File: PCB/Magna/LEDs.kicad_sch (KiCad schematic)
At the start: 90 parts, among them U2001 74HC595, U2002 74HC595, U2003 74HC595, U2004 74HC595, U2005 74HC595

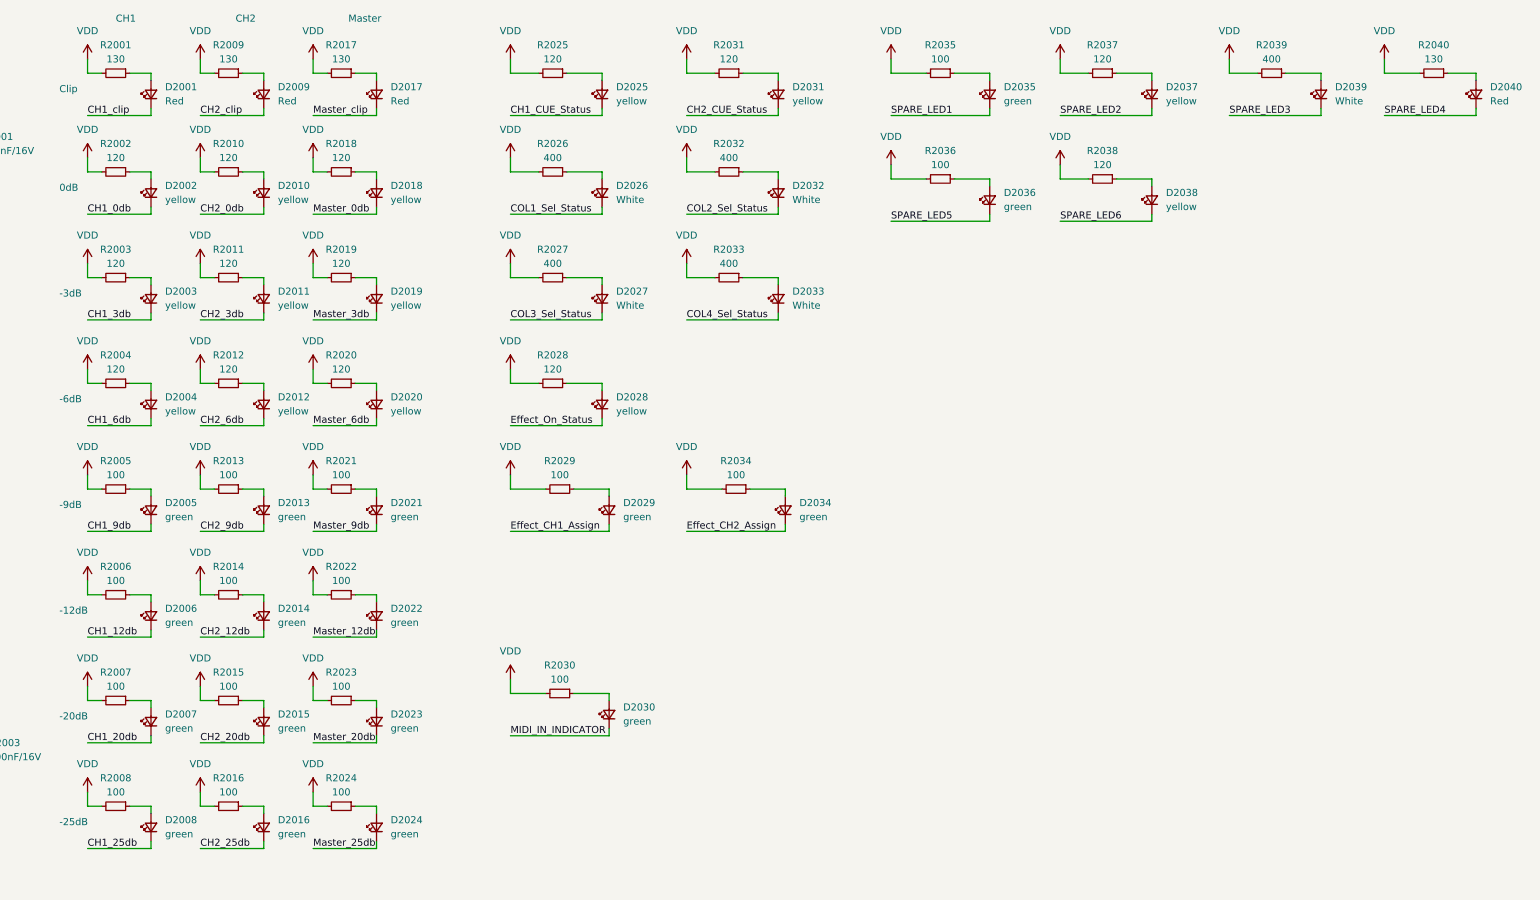
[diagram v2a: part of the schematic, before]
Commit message: Select parts for all components
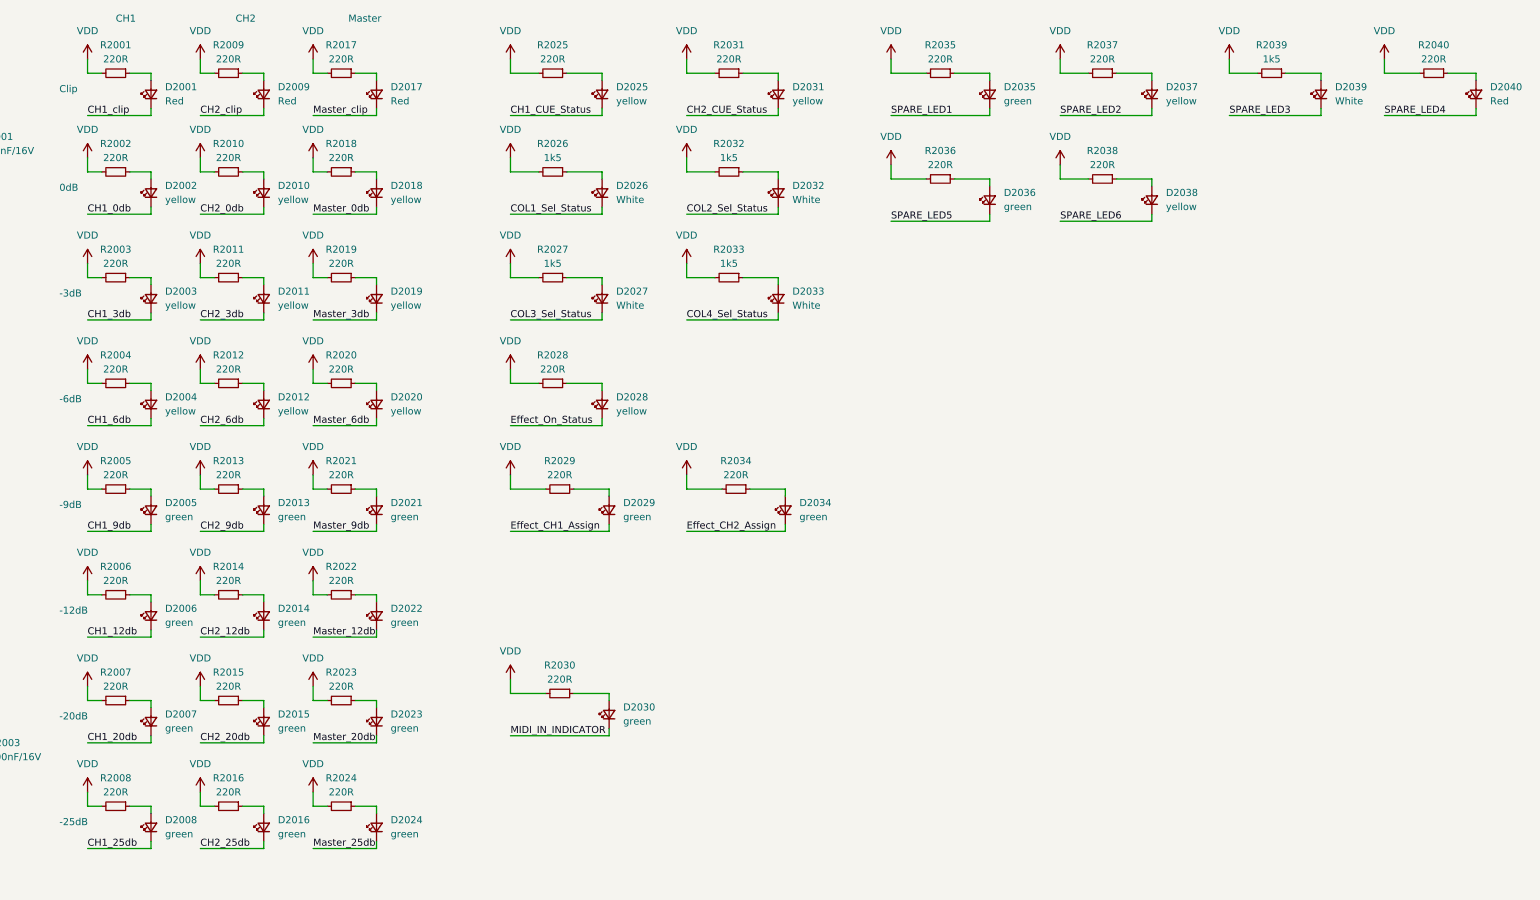
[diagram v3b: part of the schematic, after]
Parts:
- D2001, D2009, D2017, D2040: footprint (none) -> Diode_SMD:D_0805_2012Metric_Pad1.15x1.40mm_HandSolder; LCSC (none) -> C84256
- D2002, D2003, D2004, D2010, D2011, D2012, D2018, D2019, D2020, D2025, D2028, D2031, D2037, D2038: footprint (none) -> Diode_SMD:D_0805_2012Metric_Pad1.15x1.40mm_HandSolder; LCSC (none) -> C2296
- D2005, D2006, D2007, D2008, D2013, D2014, D2015, D2016, D2021, D2022, D2023, D2024, D2029, D2030, D2034, D2035, D2036: footprint (none) -> Diode_SMD:D_0805_2012Metric_Pad1.15x1.40mm_HandSolder; LCSC (none) -> C2297
- D2026, D2027, D2032, D2033, D2039: footprint (none) -> Diode_SMD:D_0805_2012Metric_Pad1.15x1.40mm_HandSolder; LCSC (none) -> C34499
- R2001, R2009, R2017, R2040: value 130 -> 220R; footprint (none) -> Resistor_SMD:R_0805_2012Metric_Pad1.20x1.40mm_HandSolder; LCSC (none) -> C17557
- R2002, R2003, R2004, R2010, R2011, R2012, R2018, R2019, R2020, R2025, R2028, R2031, R2037, R2038: value 120 -> 220R; footprint (none) -> Resistor_SMD:R_0805_2012Metric_Pad1.20x1.40mm_HandSolder; LCSC (none) -> C17557
- R2005, R2006, R2007, R2008, R2013, R2014, R2015, R2016, R2021, R2022, R2023, R2024, R2029, R2030, R2034, R2035, R2036: value 100 -> 220R; footprint (none) -> Resistor_SMD:R_0805_2012Metric_Pad1.20x1.40mm_HandSolder; LCSC (none) -> C17557
- R2026, R2027, R2032, R2033, R2039: value 400 -> 1k5; footprint (none) -> Resistor_SMD:R_0805_2012Metric_Pad1.20x1.40mm_HandSolder; LCSC (none) -> C4310
- U2001, U2002, U2003, U2004, U2005: footprint (none) -> Package_SO:SO-16_3.9x9.9mm_P1.27mm; LCSC (none) -> C93838

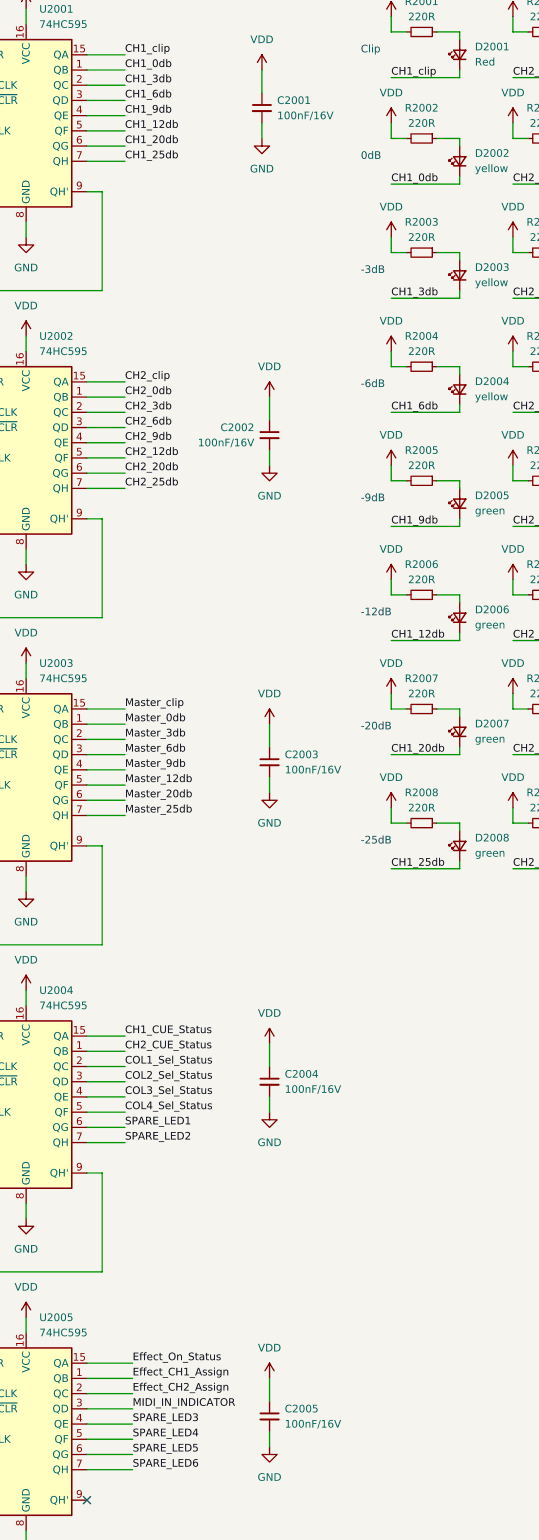
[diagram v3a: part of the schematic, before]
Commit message: Add even more component footprints and partnumbers
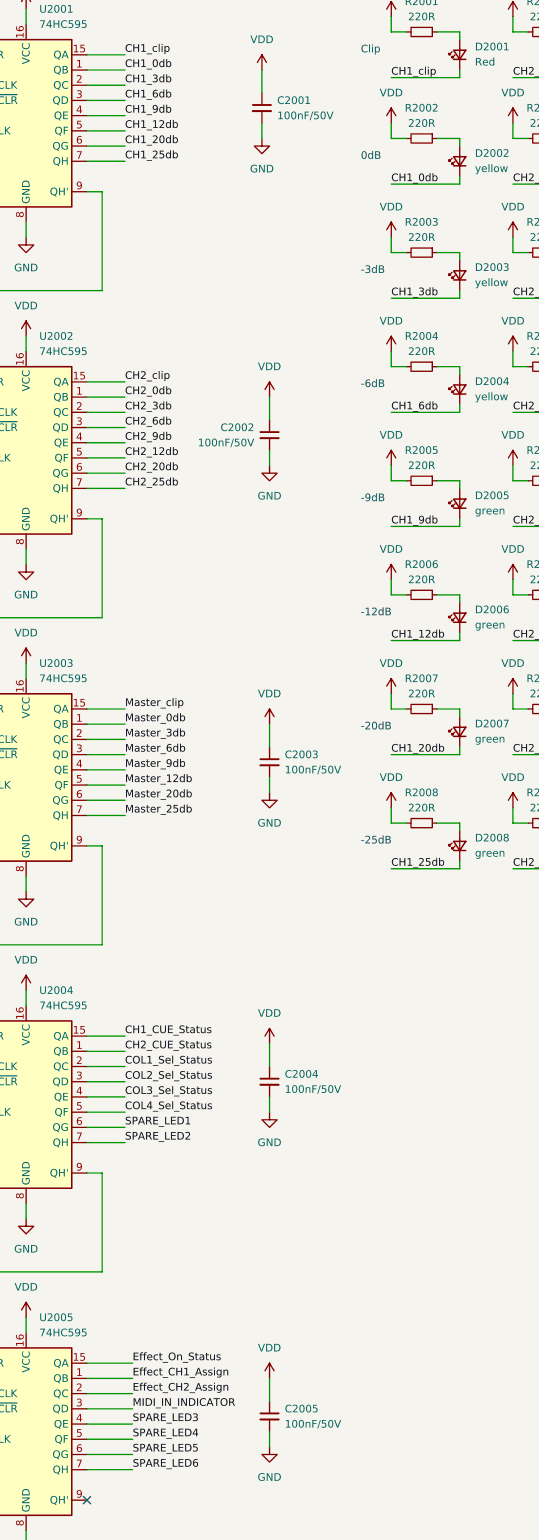
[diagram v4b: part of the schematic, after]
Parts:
- C2001, C2002, C2003, C2004, C2005: value 100nF/16V -> 100nF/50V; footprint Capacitor_SMD:C_0805_2012Metric -> Capacitor_SMD:C_0805_2012Metric_Pad1.18x1.45mm_HandSolder; LCSC C218638 -> C49678
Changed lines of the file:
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@@
       (effects (font (size 1.27 1.27)) (justify right))
     )
-    (property "Value" "100nF/16V" (at 129.54 200.6663 0)
-      (effects (font (size 1.27 1.27)) (justify right))
-    )
-    (property "Footprint" "Capacitor_SMD:C_0805_2012Metric" (at 127 199.39 0)
+    (property "Value" "100nF/50V" (at 129.54 200.6663 0)
+      (effects (font (size 1.27 1.27)) (justify right))
+    )
+    (property "Footprint" "Capacitor_SMD:C_0805_2012Metric_Pad1.18x1.45mm_HandSolder" (at 127 199.39 0)
       (effects (font (size 1.27 1.27)) hide)
     )
@@
       (effects (font (size 1.27 1.27)) hide)
     )
-    (property "LCSC" "C218638" (at 127 199.39 0)
+    (property "LCSC" "C49678" (at 127 199.39 0)
       (effects (font (size 1.27 1.27)) hide)
     )
@@
       (effects (font (size 1.27 1.27)) (justify right))
     )
-    (property "Value" "100nF/16V" (at 124.46 92.7163 0)
-      (effects (font (size 1.27 1.27)) (justify right))
-    )
-    (property "Footprint" "Capacitor_SMD:C_0805_2012Metric" (at 127 91.44 0)
+    (property "Value" "100nF/50V" (at 124.46 92.7163 0)
+      (effects (font (size 1.27 1.27)) (justify right))
+    )
+    (property "Footprint" "Capacitor_SMD:C_0805_2012Metric_Pad1.18x1.45mm_HandSolder" (at 127 91.44 0)
       (effects (font (size 1.27 1.27)) hide)
     )
@@
       (effects (font (size 1.27 1.27)) hide)
     )
-    (property "LCSC" "C218638" (at 127 91.44 0)
+    (property "LCSC" "C49678" (at 127 91.44 0)
       (effects (font (size 1.27 1.27)) hide)
     )
@@
       (effects (font (size 1.27 1.27)) (justify right))
     )
-    (property "Value" "100nF/16V" (at 129.54 256.5463 0)
-      (effects (font (size 1.27 1.27)) (justify right))
-    )
-    (property "Footprint" "Capacitor_SMD:C_0805_2012Metric" (at 127 255.27 0)
+    (property "Value" "100nF/50V" (at 129.54 256.5463 0)
+      (effects (font (size 1.27 1.27)) (justify right))
+    )
+    (property "Footprint" "Capacitor_SMD:C_0805_2012Metric_Pad1.18x1.45mm_HandSolder" (at 127 255.27 0)
       (effects (font (size 1.27 1.27)) hide)
     )
@@
       (effects (font (size 1.27 1.27)) hide)
     )
-    (property "LCSC" "C218638" (at 127 255.27 0)
+    (property "LCSC" "C49678" (at 127 255.27 0)
       (effects (font (size 1.27 1.27)) hide)
     )
@@
       (effects (font (size 1.27 1.27)) (justify right))
     )
-    (property "Value" "100nF/16V" (at 129.54 147.3263 0)
-      (effects (font (size 1.27 1.27)) (justify right))
-    )
-    (property "Footprint" "Capacitor_SMD:C_0805_2012Metric" (at 127 146.05 0)
+    (property "Value" "100nF/50V" (at 129.54 147.3263 0)
+      (effects (font (size 1.27 1.27)) (justify right))
+    )
+    (property "Footprint" "Capacitor_SMD:C_0805_2012Metric_Pad1.18x1.45mm_HandSolder" (at 127 146.05 0)
       (effects (font (size 1.27 1.27)) hide)
     )
@@
       (effects (font (size 1.27 1.27)) hide)
     )
-    (property "LCSC" "C218638" (at 127 146.05 0)
+    (property "LCSC" "C49678" (at 127 146.05 0)
       (effects (font (size 1.27 1.27)) hide)
     )
@@
       (effects (font (size 1.27 1.27)) (justify right))
     )
-    (property "Value" "100nF/16V" (at 128.27 38.1063 0)
-      (effects (font (size 1.27 1.27)) (justify right))
-    )
-    (property "Footprint" "Capacitor_SMD:C_0805_2012Metric" (at 125.73 36.83 0)
+    (property "Value" "100nF/50V" (at 128.27 38.1063 0)
+      (effects (font (size 1.27 1.27)) (justify right))
+    )
+    (property "Footprint" "Capacitor_SMD:C_0805_2012Metric_Pad1.18x1.45mm_HandSolder" (at 125.73 36.83 0)
       (effects (font (size 1.27 1.27)) hide)
     )
@@
       (effects (font (size 1.27 1.27)) hide)
     )
-    (property "LCSC" "C218638" (at 125.73 36.83 0)
-      (effects (font (size 1.27 1.27)) hide)
-    )
+    (property "LCSC" "C49678" (at 125.73 36.83 0)
+      (effects (font (size 1.27 1.27)) hide)
+    )
